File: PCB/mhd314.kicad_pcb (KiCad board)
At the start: 2 copper layers, 65.5 x 56.5 mm, 0 parts

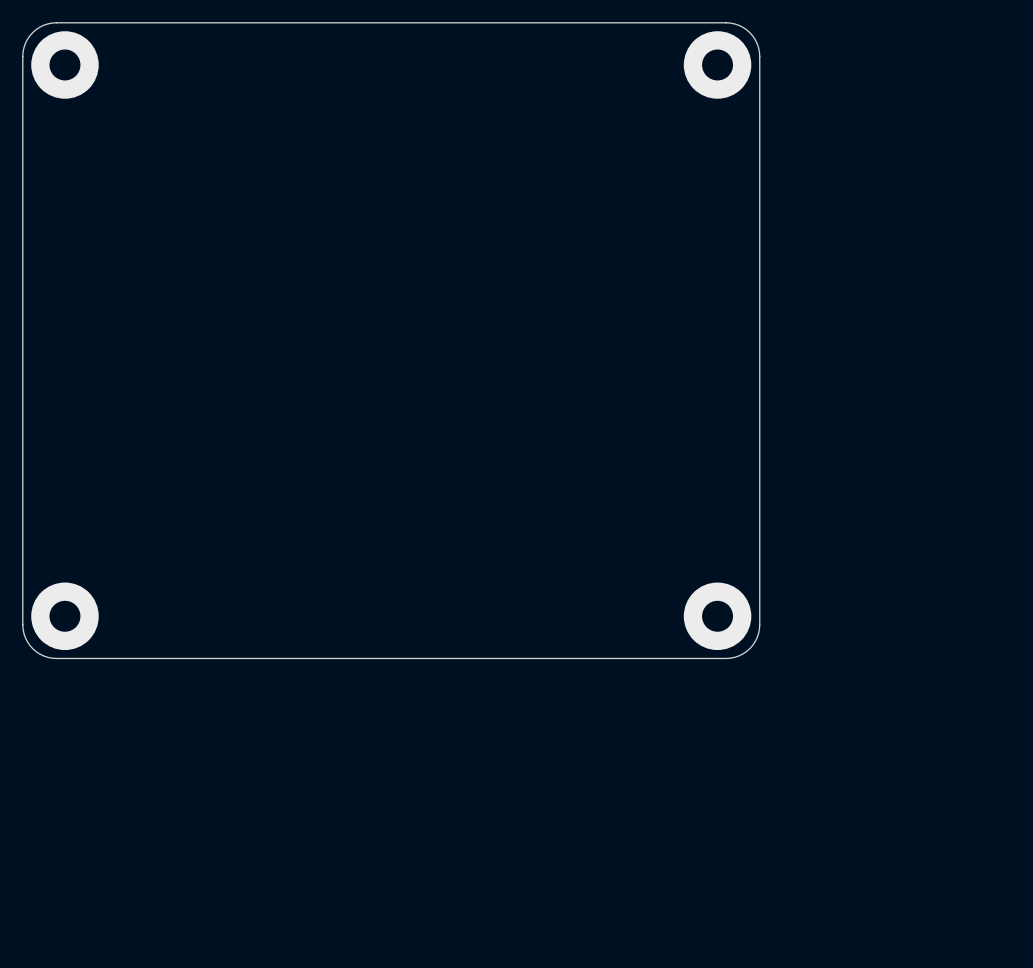
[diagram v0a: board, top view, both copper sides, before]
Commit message: Added E2P and testpoints
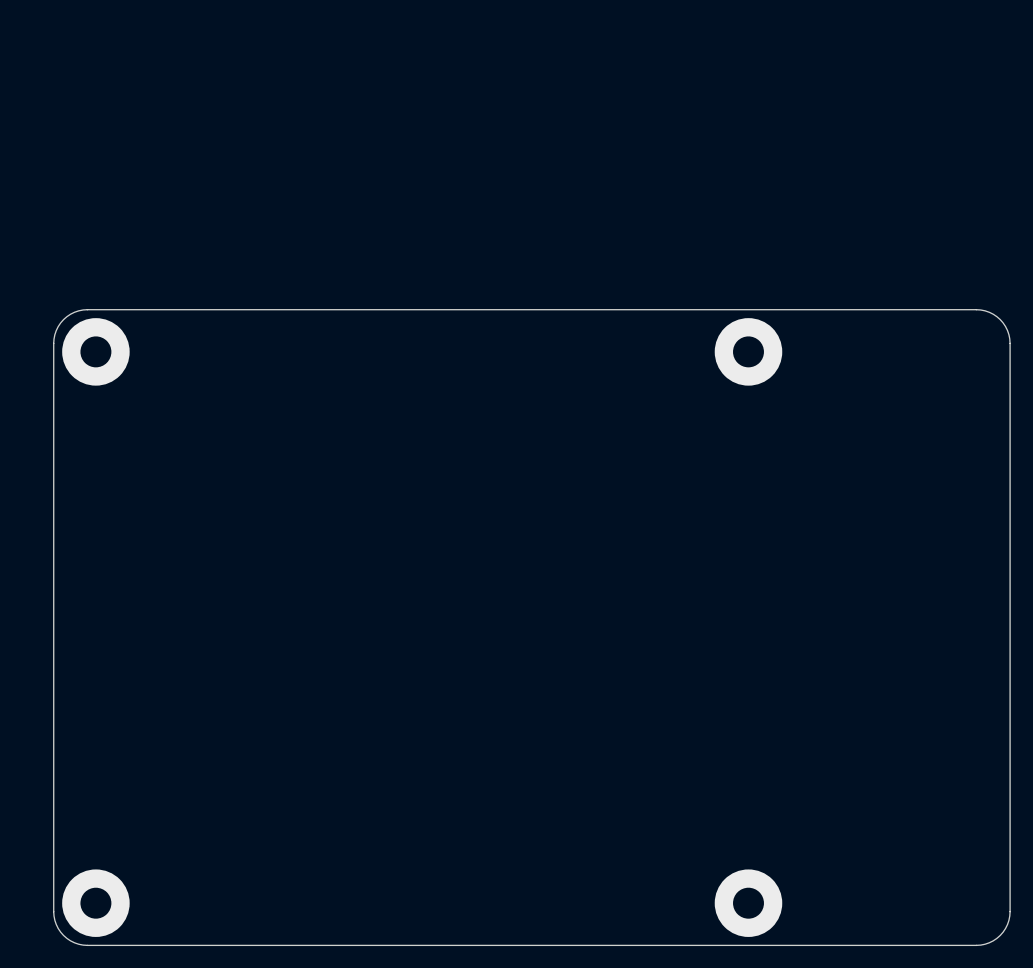
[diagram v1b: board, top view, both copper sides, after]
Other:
- board size 65.5 x 56.5 mm -> 85 x 56.5 mm
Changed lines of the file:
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@@
 	(net 0 "")
 	(gr_arc
-		(start 159.75 46.25)
-		(mid 161.87132 47.12868)
-		(end 162.75 49.25)
+		(start 182 71.75)
+		(mid 184.12132 72.62868)
+		(end 185 74.75)
 		(stroke
 			(width 0.05)
@@
 	)
 	(gr_line
-		(start 162.75 49.25)
-		(end 162.75 99.75)
+		(start 185 74.75)
+		(end 185 125.25)
 		(stroke
 			(width 0.05)
@@
 	)
 	(gr_line
-		(start 100.25 46.25)
-		(end 159.75 46.25)
+		(start 103 71.75)
+		(end 182 71.75)
 		(stroke
 			(width 0.05)
@@
 	)
 	(gr_arc
-		(start 162.75 99.75)
-		(mid 161.87132 101.87132)
-		(end 159.75 102.75)
+		(start 185 125.25)
+		(mid 184.12132 127.37132)
+		(end 182 128.25)
 		(stroke
 			(width 0.05)
@@
 	)
 	(gr_line
-		(start 159.75 102.75)
-		(end 100.25 102.75)
+		(start 182 128.25)
+		(end 103 128.25)
 		(stroke
 			(width 0.05)
@@
 	)
 	(gr_arc
-		(start 100.25 102.75)
-		(mid 98.12868 101.87132)
-		(end 97.25 99.75)
+		(start 103 128.25)
+		(mid 100.87868 127.37132)
+		(end 100 125.25)
 		(stroke
 			(width 0.05)
@@
 	)
 	(gr_arc
-		(start 97.25 49.25)
-		(mid 98.12868 47.12868)
-		(end 100.25 46.25)
+		(start 100 74.75)
+		(mid 100.87868 72.62868)
+		(end 103 71.75)
 		(stroke
 			(width 0.05)
@@
 	)
 	(gr_line
-		(start 97.25 99.75)
-		(end 97.25 49.25)
+		(start 100 125.25)
+		(end 100 74.75)
 		(stroke
 			(width 0.05)
@@
 	)
 	(via
-		(at 159 50)
+		(at 161.75 75.5)
 		(size 6)
 		(drill 2.75)
@@
 	)
 	(via
-		(at 101 50)
+		(at 103.75 75.5)
 		(size 6)
 		(drill 2.75)
@@
 	)
 	(via
-		(at 101 99)
+		(at 103.75 124.5)
 		(size 6)
 		(drill 2.75)
@@
 	)
 	(via
-		(at 159 99)
+		(at 161.75 124.5)
 		(size 6)
 		(drill 2.75)

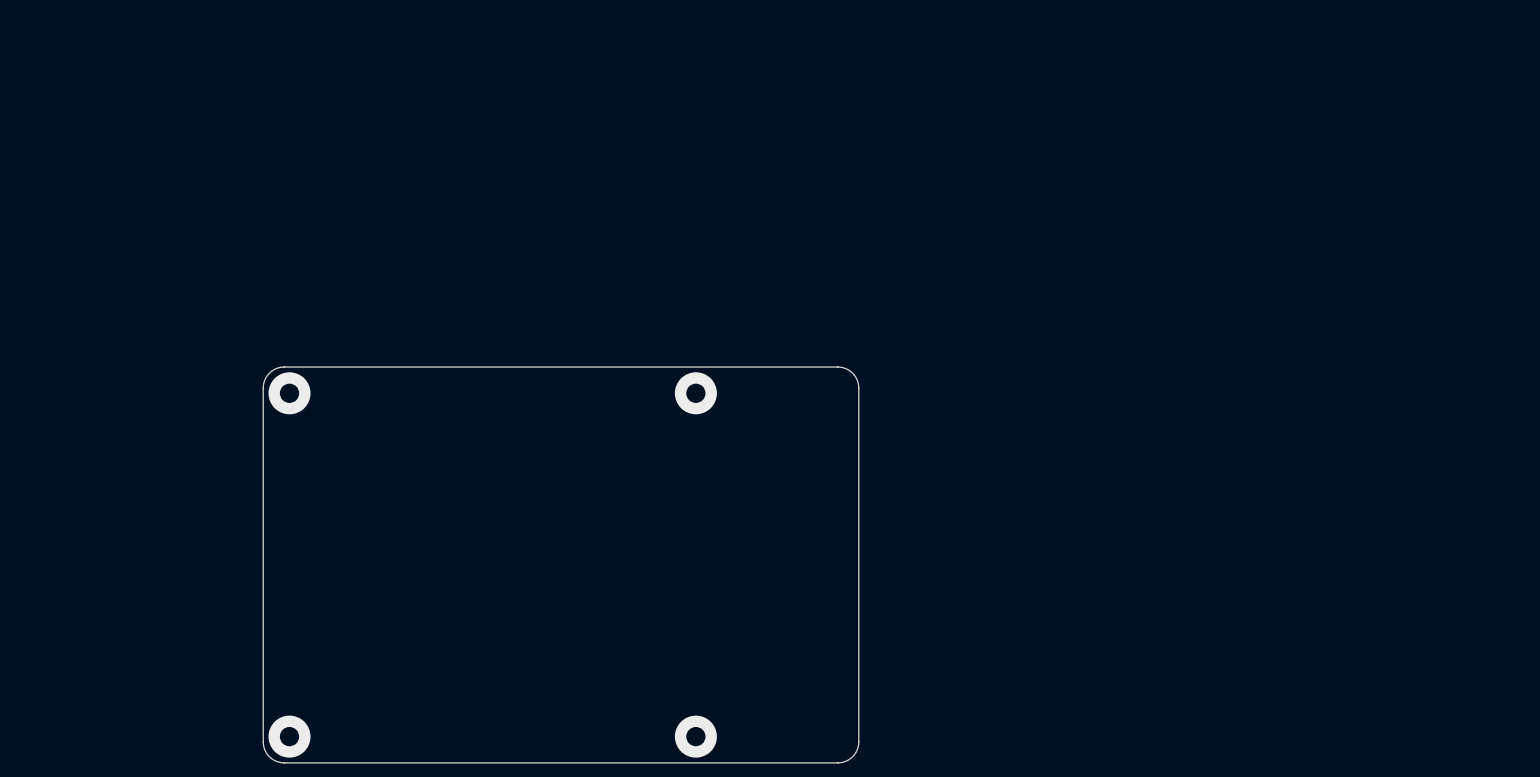
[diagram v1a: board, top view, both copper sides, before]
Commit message: PCB drawn with connector placement ok
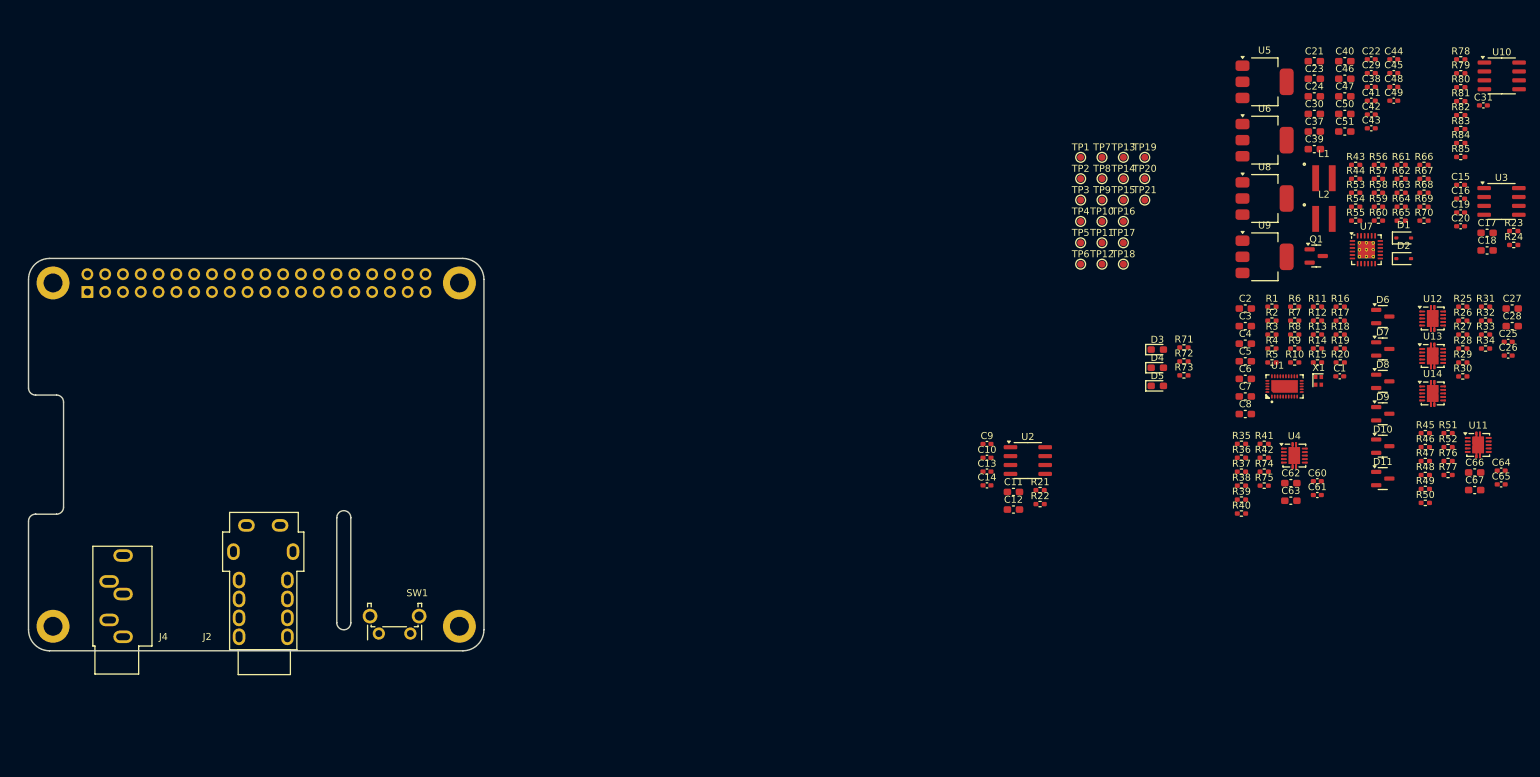
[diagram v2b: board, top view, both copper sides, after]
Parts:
- added C1: 100nF, Capacitor_SMD:C_0402_1005Metric_Pad0.74x0.62mm_HandSolder, F.Cu at (253.6, 73.1)
- added C10: 100nF, Capacitor_SMD:C_0402_1005Metric_Pad0.74x0.62mm_HandSolder, F.Cu at (203.3, 84.7)
- added C11: 1uF, Capacitor_SMD:C_0603_1608Metric_Pad1.08x0.95mm_HandSolder, F.Cu at (207.1, 89.6)
- added C12: 1uF, Capacitor_SMD:C_0603_1608Metric_Pad1.08x0.95mm_HandSolder, F.Cu at (207.1, 92.1)
- added C13: 1.2nF, Capacitor_SMD:C_0402_1005Metric_Pad0.74x0.62mm_HandSolder, F.Cu at (203.3, 86.7)
- added C14: 1.2nF, Capacitor_SMD:C_0402_1005Metric_Pad0.74x0.62mm_HandSolder, F.Cu at (203.3, 88.6)
- added C15: 100nF, Capacitor_SMD:C_0402_1005Metric_Pad0.74x0.62mm_HandSolder, F.Cu at (270.9, 45.8)
- added C16: 100nF, Capacitor_SMD:C_0402_1005Metric_Pad0.74x0.62mm_HandSolder, F.Cu at (270.9, 47.7)
- added C17: 1uF, Capacitor_SMD:C_0603_1608Metric_Pad1.08x0.95mm_HandSolder, F.Cu at (274.7, 52.6)
- added C18: 1uF, Capacitor_SMD:C_0603_1608Metric_Pad1.08x0.95mm_HandSolder, F.Cu at (274.7, 55.1)
- added C19: 1.2nF, Capacitor_SMD:C_0402_1005Metric_Pad0.74x0.62mm_HandSolder, F.Cu at (270.9, 49.7)
- added C2: 1uF, Capacitor_SMD:C_0603_1608Metric_Pad1.08x0.95mm_HandSolder, F.Cu at (240.2, 63.4)
- added C20: 1.2nF, Capacitor_SMD:C_0402_1005Metric_Pad0.74x0.62mm_HandSolder, F.Cu at (270.9, 51.7)
- added C21: 1uF, Capacitor_SMD:C_0603_1608Metric_Pad1.08x0.95mm_HandSolder, F.Cu at (250.0, 28.1)
- added C22: 100nF, Capacitor_SMD:C_0402_1005Metric_Pad0.74x0.62mm_HandSolder, F.Cu at (258.1, 27.8)
- added C23: 1uF, Capacitor_SMD:C_0603_1608Metric_Pad1.08x0.95mm_HandSolder, F.Cu at (250.0, 30.6)
- added C24: 1uF, Capacitor_SMD:C_0603_1608Metric_Pad1.08x0.95mm_HandSolder, F.Cu at (250.0, 33.1)
- added C25: 100nF, Capacitor_SMD:C_0402_1005Metric_Pad0.74x0.62mm_HandSolder, F.Cu at (277.7, 68.2)
- added C26: 100nF, Capacitor_SMD:C_0402_1005Metric_Pad0.74x0.62mm_HandSolder, F.Cu at (277.7, 70.1)
- added C27: 1uF, Capacitor_SMD:C_0603_1608Metric_Pad1.08x0.95mm_HandSolder, F.Cu at (278.3, 63.4)
- added C28: 1uF, Capacitor_SMD:C_0603_1608Metric_Pad1.08x0.95mm_HandSolder, F.Cu at (278.3, 65.9)
- added C29: 100nF, Capacitor_SMD:C_0402_1005Metric_Pad0.74x0.62mm_HandSolder, F.Cu at (258.1, 29.8)
- added C3: 1uF, Capacitor_SMD:C_0603_1608Metric_Pad1.08x0.95mm_HandSolder, F.Cu at (240.2, 65.9)
- added C30: 1uF, Capacitor_SMD:C_0603_1608Metric_Pad1.08x0.95mm_HandSolder, F.Cu at (250.0, 35.6)
- added C31: 100nF, Capacitor_SMD:C_0402_1005Metric_Pad0.74x0.62mm_HandSolder, F.Cu at (274.1, 34.4)
- added C37: 4.7uF, Capacitor_SMD:C_0603_1608Metric_Pad1.08x0.95mm_HandSolder, F.Cu at (250.0, 38.1)
- added C38: 6.8pF, Capacitor_SMD:C_0402_1005Metric_Pad0.74x0.62mm_HandSolder, F.Cu at (258.1, 31.8)
- added C39: 22uF, Capacitor_SMD:C_0603_1608Metric_Pad1.08x0.95mm_HandSolder, F.Cu at (250.0, 40.6)
- added C4: 1uF, Capacitor_SMD:C_0603_1608Metric_Pad1.08x0.95mm_HandSolder, F.Cu at (240.2, 68.4)
- added C40: 4.7uF, Capacitor_SMD:C_0603_1608Metric_Pad1.08x0.95mm_HandSolder, F.Cu at (254.4, 28.1)
- added C41: 100nF, Capacitor_SMD:C_0402_1005Metric_Pad0.74x0.62mm_HandSolder, F.Cu at (258.1, 33.7)
- added C42: 220nF, Capacitor_SMD:C_0402_1005Metric_Pad0.74x0.62mm_HandSolder, F.Cu at (258.1, 35.7)
- added C43: 7.5pF, Capacitor_SMD:C_0402_1005Metric_Pad0.74x0.62mm_HandSolder, F.Cu at (258.1, 37.7)
- added C44: 10nF, Capacitor_SMD:C_0402_1005Metric_Pad0.74x0.62mm_HandSolder, F.Cu at (261.4, 27.8)
- added C45: 4.7nF, Capacitor_SMD:C_0402_1005Metric_Pad0.74x0.62mm_HandSolder, F.Cu at (261.4, 29.8)
- added C46: 22uF, Capacitor_SMD:C_0603_1608Metric_Pad1.08x0.95mm_HandSolder, F.Cu at (254.4, 30.6)
- added C47: 22uF, Capacitor_SMD:C_0603_1608Metric_Pad1.08x0.95mm_HandSolder, F.Cu at (254.4, 33.1)
- added C48: 100nF, Capacitor_SMD:C_0402_1005Metric_Pad0.74x0.62mm_HandSolder, F.Cu at (261.4, 31.8)
- added C49: 100nF, Capacitor_SMD:C_0402_1005Metric_Pad0.74x0.62mm_HandSolder, F.Cu at (261.4, 33.7)
- added C5: 1uF, Capacitor_SMD:C_0603_1608Metric_Pad1.08x0.95mm_HandSolder, F.Cu at (240.2, 70.9)
- added C50: 1uF, Capacitor_SMD:C_0603_1608Metric_Pad1.08x0.95mm_HandSolder, F.Cu at (254.4, 35.6)
- added C51: 1uF, Capacitor_SMD:C_0603_1608Metric_Pad1.08x0.95mm_HandSolder, F.Cu at (254.4, 38.1)
- added C6: 1uF, Capacitor_SMD:C_0603_1608Metric_Pad1.08x0.95mm_HandSolder, F.Cu at (240.2, 73.4)
- added C60: 100nF, Capacitor_SMD:C_0402_1005Metric_Pad0.74x0.62mm_HandSolder, F.Cu at (250.4, 88.0)
- added C61: 100nF, Capacitor_SMD:C_0402_1005Metric_Pad0.74x0.62mm_HandSolder, F.Cu at (250.4, 90.0)
- added C62: 1uF, Capacitor_SMD:C_0603_1608Metric_Pad1.08x0.95mm_HandSolder, F.Cu at (246.7, 88.3)
- added C63: 1uF, Capacitor_SMD:C_0603_1608Metric_Pad1.08x0.95mm_HandSolder, F.Cu at (246.7, 90.8)
- added C64: 100nF, Capacitor_SMD:C_0402_1005Metric_Pad0.74x0.62mm_HandSolder, F.Cu at (276.7, 86.5)
- added C65: 100nF, Capacitor_SMD:C_0402_1005Metric_Pad0.74x0.62mm_HandSolder, F.Cu at (276.7, 88.5)
- added C66: 1uF, Capacitor_SMD:C_0603_1608Metric_Pad1.08x0.95mm_HandSolder, F.Cu at (272.9, 86.8)
- added C67: 1uF, Capacitor_SMD:C_0603_1608Metric_Pad1.08x0.95mm_HandSolder, F.Cu at (272.9, 89.3)
- added C7: 1uF, Capacitor_SMD:C_0603_1608Metric_Pad1.08x0.95mm_HandSolder, F.Cu at (240.2, 76.0)
- added C8: 1uF, Capacitor_SMD:C_0603_1608Metric_Pad1.08x0.95mm_HandSolder, F.Cu at (240.2, 78.5)
- added C9: 100nF, Capacitor_SMD:C_0402_1005Metric_Pad0.74x0.62mm_HandSolder, F.Cu at (203.3, 82.7)
- added D1: 1N5819WS, Diode_SMD:D_SOD-323, F.Cu at (262.8, 53.3)
- added D10: BAV99, Package_TO_SOT_SMD:SOT-23, F.Cu at (259.8, 83.0)
- added D11: BAV99, Package_TO_SOT_SMD:SOT-23, F.Cu at (259.8, 87.7)
- added D2: 1N5819WS, Diode_SMD:D_SOD-323, F.Cu at (262.8, 56.3)
- added D3: LED, LED_SMD:LED_0603_1608Metric_Pad1.05x0.95mm_HandSolder, F.Cu at (227.6, 69.3)
- added D4: LED, LED_SMD:LED_0603_1608Metric_Pad1.05x0.95mm_HandSolder, F.Cu at (227.6, 71.8)
- added D5: LED, LED_SMD:LED_0603_1608Metric_Pad1.05x0.95mm_HandSolder, F.Cu at (227.6, 74.4)
- added D6: BAV99, Package_TO_SOT_SMD:SOT-23, F.Cu at (259.8, 64.5)
- added D7: BAV99, Package_TO_SOT_SMD:SOT-23, F.Cu at (259.8, 69.2)
- added D8: BAV99, Package_TO_SOT_SMD:SOT-23, F.Cu at (259.8, 73.8)
- added D9: BAV99, Package_TO_SOT_SMD:SOT-23, F.Cu at (259.8, 78.4)
- added H1: MountingHole, MountingHole:MountingHole_2.7mm_M2.5_DIN965_Pad, F.Cu at (70.0, 59.8)
- added H2: MountingHole, MountingHole:MountingHole_2.7mm_M2.5_DIN965_Pad, F.Cu at (128.0, 59.8)
- added H3: MountingHole, MountingHole:MountingHole_2.7mm_M2.5_DIN965_Pad, F.Cu at (70.0, 108.8)
- added H4: MountingHole, MountingHole:MountingHole_2.7mm_M2.5_DIN965_Pad, F.Cu at (128.0, 108.8)
- added J1: Raspberry_Pi_2_3, Connector_PinSocket_2.54mm:PinSocket_2x20_P2.54mm_Vertical, B.Cu at (74.9, 61.0)
- added J2: AudioJack_Pentaconn, _mahaudio KiCad Library:Jack_4.4mm_Pentaconn_NBA1-24-001_Horizontal, F.Cu at (100.0, 98.1)
- added J4: AudioJack3_SwitchTR, _mahaudio KiCad Library:Jack_3.5mm_CUI_SJ1-3535NG_Horizontal_3D, F.Cu at (80.0, 110.2)
- added L1: 4.7uH, LIB:WE-MAPI_4030, F.Cu at (251.4, 44.8)
- added L2: 4.7uH, LIB:WE-MAPI_4030, F.Cu at (251.4, 50.6)
- added Q1: AO3401A, Package_TO_SOT_SMD:SOT-23, F.Cu at (250.3, 55.9)
- added R1: 20R, Resistor_SMD:R_0402_1005Metric_Pad0.72x0.64mm_HandSolder, F.Cu at (244.0, 63.1)
- added R10: 10k, Resistor_SMD:R_0402_1005Metric_Pad0.72x0.64mm_HandSolder, F.Cu at (247.2, 71.1)
- added R11: 10k, Resistor_SMD:R_0402_1005Metric_Pad0.72x0.64mm_HandSolder, F.Cu at (250.5, 63.1)
- added R12: 10k, Resistor_SMD:R_0402_1005Metric_Pad0.72x0.64mm_HandSolder, F.Cu at (250.5, 65.1)
- added R13: 20R, Resistor_SMD:R_0402_1005Metric_Pad0.72x0.64mm_HandSolder, F.Cu at (250.5, 67.1)
- added R14: 100k, Resistor_SMD:R_0402_1005Metric_Pad0.72x0.64mm_HandSolder, F.Cu at (250.5, 69.1)
- added R15: 10k, Resistor_SMD:R_0402_1005Metric_Pad0.72x0.64mm_HandSolder, F.Cu at (250.5, 71.1)
- added R16: 10k, Resistor_SMD:R_0402_1005Metric_Pad0.72x0.64mm_HandSolder, F.Cu at (253.7, 63.1)
- added R17: 0R, Resistor_SMD:R_0402_1005Metric_Pad0.72x0.64mm_HandSolder, F.Cu at (253.7, 65.1)
- added R18: 0R, Resistor_SMD:R_0402_1005Metric_Pad0.72x0.64mm_HandSolder, F.Cu at (253.7, 67.1)
- added R19: 0R, Resistor_SMD:R_0402_1005Metric_Pad0.72x0.64mm_HandSolder, F.Cu at (253.7, 69.1)
- added R2: 20R, Resistor_SMD:R_0402_1005Metric_Pad0.72x0.64mm_HandSolder, F.Cu at (244.0, 65.1)
- added R20: 0R, Resistor_SMD:R_0402_1005Metric_Pad0.72x0.64mm_HandSolder, F.Cu at (253.7, 71.1)
- added R21: 1.05k, Resistor_SMD:R_0402_1005Metric_Pad0.72x0.64mm_HandSolder, F.Cu at (210.9, 89.3)
- added R22: 1.05k, Resistor_SMD:R_0402_1005Metric_Pad0.72x0.64mm_HandSolder, F.Cu at (210.9, 91.3)
- added R23: 1.05k, Resistor_SMD:R_0402_1005Metric_Pad0.72x0.64mm_HandSolder, F.Cu at (278.5, 52.3)
- added R24: 1.05k, Resistor_SMD:R_0402_1005Metric_Pad0.72x0.64mm_HandSolder, F.Cu at (278.5, 54.3)
- added R25: 481R, Resistor_SMD:R_0402_1005Metric_Pad0.72x0.64mm_HandSolder, F.Cu at (271.2, 63.1)
- added R26: 481R, Resistor_SMD:R_0402_1005Metric_Pad0.72x0.64mm_HandSolder, F.Cu at (271.2, 65.1)
- added R27: 336R, Resistor_SMD:R_0402_1005Metric_Pad0.72x0.64mm_HandSolder, F.Cu at (271.2, 67.1)
- added R28: 336R, Resistor_SMD:R_0402_1005Metric_Pad0.72x0.64mm_HandSolder, F.Cu at (271.2, 69.1)
- added R29: 481R, Resistor_SMD:R_0402_1005Metric_Pad0.72x0.64mm_HandSolder, F.Cu at (271.2, 71.1)
- added R3: 20R, Resistor_SMD:R_0402_1005Metric_Pad0.72x0.64mm_HandSolder, F.Cu at (244.0, 67.1)
- added R30: 481R, Resistor_SMD:R_0402_1005Metric_Pad0.72x0.64mm_HandSolder, F.Cu at (271.2, 73.1)
- added R31: 336R, Resistor_SMD:R_0402_1005Metric_Pad0.72x0.64mm_HandSolder, F.Cu at (274.5, 63.1)
- added R32: 336R, Resistor_SMD:R_0402_1005Metric_Pad0.72x0.64mm_HandSolder, F.Cu at (274.5, 65.1)
- added R33: 10k, Resistor_SMD:R_0402_1005Metric_Pad0.72x0.64mm_HandSolder, F.Cu at (274.5, 67.1)
- added R34: 20R, Resistor_SMD:R_0402_1005Metric_Pad0.72x0.64mm_HandSolder, F.Cu at (274.5, 69.1)
- added R35: 481R, Resistor_SMD:R_0402_1005Metric_Pad0.72x0.64mm_HandSolder, F.Cu at (239.6, 82.7)
- added R36: 481R, Resistor_SMD:R_0402_1005Metric_Pad0.72x0.64mm_HandSolder, F.Cu at (239.6, 84.7)
- added R37: 174R, Resistor_SMD:R_0402_1005Metric_Pad0.72x0.64mm_HandSolder, F.Cu at (239.6, 86.7)
- added R38: 174R, Resistor_SMD:R_0402_1005Metric_Pad0.72x0.64mm_HandSolder, F.Cu at (239.6, 88.7)
- added R39: 481R, Resistor_SMD:R_0402_1005Metric_Pad0.72x0.64mm_HandSolder, F.Cu at (239.6, 90.7)
- added R4: 20R, Resistor_SMD:R_0402_1005Metric_Pad0.72x0.64mm_HandSolder, F.Cu at (244.0, 69.1)
- added R40: 481R, Resistor_SMD:R_0402_1005Metric_Pad0.72x0.64mm_HandSolder, F.Cu at (239.6, 92.7)
- added R41: 174R, Resistor_SMD:R_0402_1005Metric_Pad0.72x0.64mm_HandSolder, F.Cu at (242.9, 82.7)
- added R42: 174R, Resistor_SMD:R_0402_1005Metric_Pad0.72x0.64mm_HandSolder, F.Cu at (242.9, 84.7)
- added R43: 390R, Resistor_SMD:R_0402_1005Metric_Pad0.72x0.64mm_HandSolder, F.Cu at (255.9, 42.9)
- added R44: 240R, Resistor_SMD:R_0402_1005Metric_Pad0.72x0.64mm_HandSolder, F.Cu at (255.9, 44.9)
- added R45: 481R, Resistor_SMD:R_0402_1005Metric_Pad0.72x0.64mm_HandSolder, F.Cu at (265.9, 81.2)
- added R46: 481R, Resistor_SMD:R_0402_1005Metric_Pad0.72x0.64mm_HandSolder, F.Cu at (265.9, 83.2)
- added R47: 481R, Resistor_SMD:R_0402_1005Metric_Pad0.72x0.64mm_HandSolder, F.Cu at (265.9, 85.2)
- added R48: 481R, Resistor_SMD:R_0402_1005Metric_Pad0.72x0.64mm_HandSolder, F.Cu at (265.9, 87.2)
- added R49: 174R, Resistor_SMD:R_0402_1005Metric_Pad0.72x0.64mm_HandSolder, F.Cu at (265.9, 89.2)
- added R5: 0R, Resistor_SMD:R_0402_1005Metric_Pad0.72x0.64mm_HandSolder, F.Cu at (244.0, 71.1)
- added R50: 174R, Resistor_SMD:R_0402_1005Metric_Pad0.72x0.64mm_HandSolder, F.Cu at (265.9, 91.1)
- added R51: 174R, Resistor_SMD:R_0402_1005Metric_Pad0.72x0.64mm_HandSolder, F.Cu at (269.1, 81.2)
- added R52: 174R, Resistor_SMD:R_0402_1005Metric_Pad0.72x0.64mm_HandSolder, F.Cu at (269.1, 83.2)
- added R53: 390R, Resistor_SMD:R_0402_1005Metric_Pad0.72x0.64mm_HandSolder, F.Cu at (255.9, 46.9)
- added R54: 240R, Resistor_SMD:R_0402_1005Metric_Pad0.72x0.64mm_HandSolder, F.Cu at (255.9, 48.9)
- added R55: 1M, Resistor_SMD:R_0402_1005Metric_Pad0.72x0.64mm_HandSolder, F.Cu at (255.9, 50.9)
- added R56: 178k, Resistor_SMD:R_0402_1005Metric_Pad0.72x0.64mm_HandSolder, F.Cu at (259.2, 42.9)
- added R57: 100R, Resistor_SMD:R_0402_1005Metric_Pad0.72x0.64mm_HandSolder, F.Cu at (259.2, 44.9)
- added R58: 150k, Resistor_SMD:R_0402_1005Metric_Pad0.72x0.64mm_HandSolder, F.Cu at (259.2, 46.9)
- added R59: 1M, Resistor_SMD:R_0402_1005Metric_Pad0.72x0.64mm_HandSolder, F.Cu at (259.2, 48.9)
- added R6: 0R, Resistor_SMD:R_0402_1005Metric_Pad0.72x0.64mm_HandSolder, F.Cu at (247.2, 63.1)
- added R60: 720R, Resistor_SMD:R_0402_1005Metric_Pad0.72x0.64mm_HandSolder, F.Cu at (259.2, 50.9)
- added R61: 720R, Resistor_SMD:R_0402_1005Metric_Pad0.72x0.64mm_HandSolder, F.Cu at (262.4, 42.9)
- added R62: 240R, Resistor_SMD:R_0402_1005Metric_Pad0.72x0.64mm_HandSolder, F.Cu at (262.4, 44.9)
- added R63: 240R, Resistor_SMD:R_0402_1005Metric_Pad0.72x0.64mm_HandSolder, F.Cu at (262.4, 46.9)
- added R64: 0R, Resistor_SMD:R_0402_1005Metric_Pad0.72x0.64mm_HandSolder, F.Cu at (262.4, 48.9)
- added R65: 0R, Resistor_SMD:R_0402_1005Metric_Pad0.72x0.64mm_HandSolder, F.Cu at (262.4, 50.9)
- added R66: 0R, Resistor_SMD:R_0402_1005Metric_Pad0.72x0.64mm_HandSolder, F.Cu at (265.7, 42.9)
- added R67: 0R, Resistor_SMD:R_0402_1005Metric_Pad0.72x0.64mm_HandSolder, F.Cu at (265.7, 44.9)
- added R68: 0R, Resistor_SMD:R_0402_1005Metric_Pad0.72x0.64mm_HandSolder, F.Cu at (265.7, 46.9)
- added R69: 0R, Resistor_SMD:R_0402_1005Metric_Pad0.72x0.64mm_HandSolder, F.Cu at (265.7, 48.9)
- added R7: 0R, Resistor_SMD:R_0402_1005Metric_Pad0.72x0.64mm_HandSolder, F.Cu at (247.2, 65.1)
- added R70: 0R, Resistor_SMD:R_0402_1005Metric_Pad0.72x0.64mm_HandSolder, F.Cu at (265.7, 50.9)
- added R71: 720R, Resistor_SMD:R_0402_1005Metric_Pad0.72x0.64mm_HandSolder, F.Cu at (231.4, 69.0)
- added R72: 720R, Resistor_SMD:R_0402_1005Metric_Pad0.72x0.64mm_HandSolder, F.Cu at (231.4, 71.0)
- added R73: 720R, Resistor_SMD:R_0402_1005Metric_Pad0.72x0.64mm_HandSolder, F.Cu at (231.4, 72.9)
- added R74: 10k, Resistor_SMD:R_0402_1005Metric_Pad0.72x0.64mm_HandSolder, F.Cu at (242.9, 86.7)
- added R75: 20R, Resistor_SMD:R_0402_1005Metric_Pad0.72x0.64mm_HandSolder, F.Cu at (242.9, 88.7)
- added R76: 10k, Resistor_SMD:R_0402_1005Metric_Pad0.72x0.64mm_HandSolder, F.Cu at (269.1, 85.2)
- added R77: 20R, Resistor_SMD:R_0402_1005Metric_Pad0.72x0.64mm_HandSolder, F.Cu at (269.1, 87.2)
- added R78: 10k, Resistor_SMD:R_0402_1005Metric_Pad0.72x0.64mm_HandSolder, F.Cu at (270.9, 27.8)
- added R79: 10k, Resistor_SMD:R_0402_1005Metric_Pad0.72x0.64mm_HandSolder, F.Cu at (270.9, 29.8)
- added R8: 2k, Resistor_SMD:R_0402_1005Metric_Pad0.72x0.64mm_HandSolder, F.Cu at (247.2, 67.1)
- added R80: 10k, Resistor_SMD:R_0402_1005Metric_Pad0.72x0.64mm_HandSolder, F.Cu at (270.9, 31.8)
- added R81: 10k, Resistor_SMD:R_0402_1005Metric_Pad0.72x0.64mm_HandSolder, F.Cu at (270.9, 33.8)
- added R82: 10k, Resistor_SMD:R_0402_1005Metric_Pad0.72x0.64mm_HandSolder, F.Cu at (270.9, 35.8)
- added R83: 10k, Resistor_SMD:R_0402_1005Metric_Pad0.72x0.64mm_HandSolder, F.Cu at (270.9, 37.8)
- added R84: 2k, Resistor_SMD:R_0402_1005Metric_Pad0.72x0.64mm_HandSolder, F.Cu at (270.9, 39.8)
- added R85: 2k, Resistor_SMD:R_0402_1005Metric_Pad0.72x0.64mm_HandSolder, F.Cu at (270.9, 41.8)
- added R9: 2k, Resistor_SMD:R_0402_1005Metric_Pad0.72x0.64mm_HandSolder, F.Cu at (247.2, 69.1)
- added SW1: SW_Push, Button_Switch_THT:SW_Tactile_SPST_Angled_PTS645Vx39-2LFS, F.Cu at (121.0, 109.8)
- added TP1: TestPoint, TestPoint:TestPoint_Pad_D1.0mm, F.Cu at (216.7, 41.8)
- added TP10: TestPoint, TestPoint:TestPoint_Pad_D1.0mm, F.Cu at (219.7, 51.0)
- added TP11: TestPoint, TestPoint:TestPoint_Pad_D1.0mm, F.Cu at (219.7, 54.0)
- added TP12: TestPoint, TestPoint:TestPoint_Pad_D1.0mm, F.Cu at (219.7, 57.1)
- added TP13: TestPoint, TestPoint:TestPoint_Pad_D1.0mm, F.Cu at (222.8, 41.8)
- added TP14: TestPoint, TestPoint:TestPoint_Pad_D1.0mm, F.Cu at (222.8, 44.9)
- added TP15: TestPoint, TestPoint:TestPoint_Pad_D1.0mm, F.Cu at (222.8, 47.9)
- added TP16: TestPoint, TestPoint:TestPoint_Pad_D1.0mm, F.Cu at (222.8, 51.0)
- added TP17: TestPoint, TestPoint:TestPoint_Pad_D1.0mm, F.Cu at (222.8, 54.0)
- added TP18: TestPoint, TestPoint:TestPoint_Pad_D1.0mm, F.Cu at (222.8, 57.1)
- added TP19: TestPoint, TestPoint:TestPoint_Pad_D1.0mm, F.Cu at (225.8, 41.8)
- added TP2: TestPoint, TestPoint:TestPoint_Pad_D1.0mm, F.Cu at (216.7, 44.9)
- added TP20: TestPoint, TestPoint:TestPoint_Pad_D1.0mm, F.Cu at (225.8, 44.9)
- added TP21: TestPoint, TestPoint:TestPoint_Pad_D1.0mm, F.Cu at (225.8, 47.9)
- added TP3: TestPoint, TestPoint:TestPoint_Pad_D1.0mm, F.Cu at (216.7, 47.9)
- added TP4: TestPoint, TestPoint:TestPoint_Pad_D1.0mm, F.Cu at (216.7, 51.0)
- added TP5: TestPoint, TestPoint:TestPoint_Pad_D1.0mm, F.Cu at (216.7, 54.0)
- added TP6: TestPoint, TestPoint:TestPoint_Pad_D1.0mm, F.Cu at (216.7, 57.1)
- added TP7: TestPoint, TestPoint:TestPoint_Pad_D1.0mm, F.Cu at (219.7, 41.8)
- added TP8: TestPoint, TestPoint:TestPoint_Pad_D1.0mm, F.Cu at (219.7, 44.9)
- added TP9: TestPoint, TestPoint:TestPoint_Pad_D1.0mm, F.Cu at (219.7, 47.9)
- added U1: ES9038Q2M, _mahaudio KiCad Library:QFN-30_EP_3x5_Pitch0.4mm, F.Cu at (245.8, 74.5)
- added U10: AT24CS64-SSHM, Package_SO:SOIC-8_3.9x4.9mm_P1.27mm, F.Cu at (276.8, 30.2)
- added U11: OPA1622, Package_SON:Texas_S-PVSON-N10, F.Cu at (273.4, 82.9)
- added U12: OPA1622, Package_SON:Texas_S-PVSON-N10, F.Cu at (266.9, 64.8)
- added U13: OPA1622, Package_SON:Texas_S-PVSON-N10, F.Cu at (266.9, 70.2)
- added U14: OPA1622, Package_SON:Texas_S-PVSON-N10, F.Cu at (266.9, 75.5)
- added U2: OPA1612AxD, Package_SO:SOIC-8_3.9x4.9mm_P1.27mm, F.Cu at (209.1, 85.1)
- added U3: OPA1612AxD, Package_SO:SOIC-8_3.9x4.9mm_P1.27mm, F.Cu at (276.7, 48.1)
- added U4: OPA1622, Package_SON:Texas_S-PVSON-N10, F.Cu at (247.2, 84.4)
- added U5: LM317_SOT-223, Package_TO_SOT_SMD:SOT-223-3_TabPin2, F.Cu at (242.9, 31.0)
- added U6: LM317_SOT-223, Package_TO_SOT_SMD:SOT-223-3_TabPin2, F.Cu at (242.9, 39.4)
- added U7: TPS65131RGE, Package_DFN_QFN:VQFN-24-1EP_4x4mm_P0.5mm_EP2.45x2.45mm_ThermalVias, F.Cu at (257.4, 55.0)
- added U8: LM317_SOT-223, Package_TO_SOT_SMD:SOT-223-3_TabPin2, F.Cu at (242.9, 47.7)
- added U9: LM337_SOT223, Package_TO_SOT_SMD:SOT-223-3_TabPin2, F.Cu at (242.9, 56.0)
- added X1: ASCO, Oscillator:Oscillator_SMD_Abracon_ASCO-4Pin_1.6x1.2mm, F.Cu at (250.6, 73.7)
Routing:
- net (no net): vias 4 -> 0
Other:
- board size 85 x 56.5 mm -> 65 x 56 mm
- copper layers 2 -> 4

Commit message: Started placement, current with Live 20
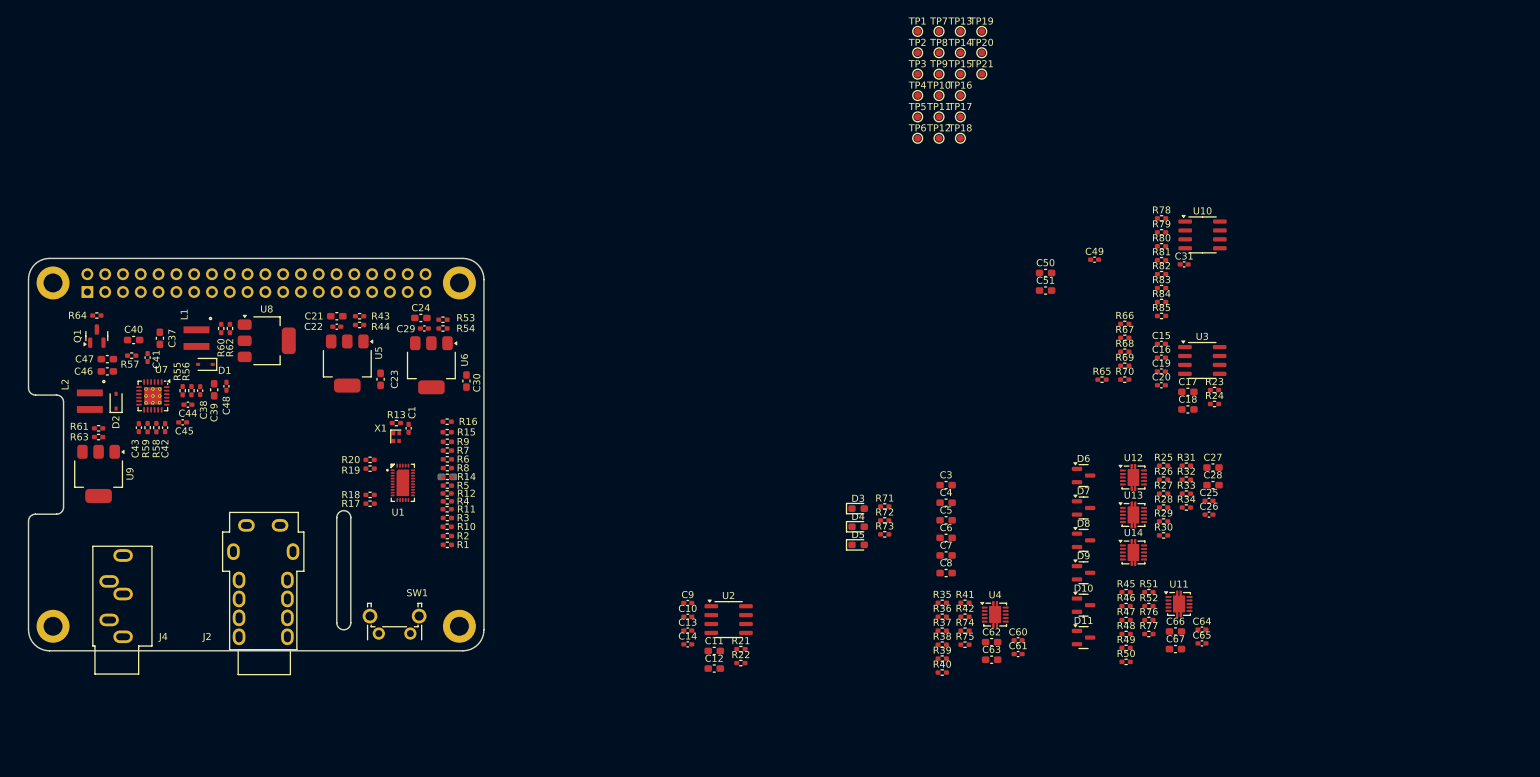
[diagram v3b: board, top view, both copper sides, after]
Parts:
- C2: moved to B.Cu
- moved R61 189.7 mm to (76.5, 80.5)
- moved R63 189.2 mm to (76.5, 81.8), turned to 180 degrees
- moved R64 186.8 mm to (76.2, 64.4), turned to 180 degrees
- moved D2 184.9 mm to (79.0, 76.6), turned to 90 degrees
- moved C46 181.5 mm to (77.8, 72.4), turned to 180 degrees
- moved C43 181.0 mm to (82.2, 80.4), turned to 90 degrees
- moved C47 180.6 mm to (77.8, 70.6), turned to 180 degrees
- moved C45 179.9 mm to (88.5, 79.7)
- moved R57 179.7 mm to (81.2, 70.1)
- moved C44 179.0 mm to (89.2, 77.1)
- moved R59 178.5 mm to (83.5, 80.4), turned to 90 degrees
- moved C41 178.4 mm to (83.5, 70.4), turned to 90 degrees
- moved L2 178.0 mm to (75.2, 76.6), turned to -90 degrees
- moved C42 177.8 mm to (86.0, 80.4), turned to -90 degrees
- moved R58 177.6 mm to (84.8, 80.4), turned to 90 degrees
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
